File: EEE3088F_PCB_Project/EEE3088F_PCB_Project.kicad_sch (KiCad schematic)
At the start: 47 parts, among them IC1 DRV8833PWPR, IC2 DRV8833PWPR, IC3 TPS62067DSGR, IC4 TPS62067DSGR, IC5 INA219AIDCNR, IC6 XL1509-5.0E1, IC7 TPS61088RHLR, J1 Conn_02x16_Odd_Even, Q1 AO3400A, Q2 AO3400A, Q5 AO3401A, Q6 AO3401A

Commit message: v0.8
- updated voltage regulation circuit (still adjusting component values)
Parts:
- removed IC6: XL1509-5.0E1, SOIC127P600X175-8N, symbol XL1509-5_0E1:XL1509-5.0E1
- added C15: 47n, CAPC1608X90N, symbol CL10B473KB8NNNC:CL10B473KB8NNNC
- added C16, C17, C21, C22, C23, C24: C_Small, symbol Device:C_Small
- added C18, C19, C7: 100n, CAPC3216X100N, symbol CL31B104KBCNNNC:CL31B104KBCNNNC
- added C2: 2.2µ, CAPC3216X180N, symbol CL31B225KBHNNNE:CL31B225KBHNNNE
- added C20: 10µ, CAPC3216X180N, symbol CL31A106KBHNNNE:CL31A106KBHNNNE
- added L2: 1.2µ, symbol Device:L_Small
- added R10: 100k, 1206W4F1003T5E:RESC3115X65N, symbol 1206W4F1003T5E:1206W4F1003T5E
- added R11, R16: R_Small_US, symbol Device:R_Small_US
- added R12: 255k, symbol Device:R_Small_US
- added R13: 56k, symbol Device:R_Small_US
- J1: now left out of the parts list
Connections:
- net 3V3 OUT: now also C7.1; no longer IC5.4 (VS)
- net 5V OUT: now also IC7.14 (VOUT_1), C21.1, C22.1, C23.1, C24.1, R16.1
- net BATTERY: now also IC7.2 (EN), IC7.9 (VBN), C18.2, C20.1, L2.2
- net GND: now also IC7.11 (NC_1), IC7.12 (NC_2), IC7.13 (MODE), IC7.20 (AGND), IC7.21 (PGND), C15.1, C17.1, C18.1, C2.1, C20.2, C21.2, C22.2, C23.2, C24.2, R10.1, R13.1
- net at IC7.1 (VCC): now also C2.2
- net at IC7.10 (SS): now also C15.2
- net at IC7.17 (FB): now also R13.2, R16.2
- net at IC7.18 (COMP): now also C16.2, R11.2
- net at IC7.19 (ILIM): now also R10.2
- net at IC7.3 (FSW): now also R12.1
- net at IC7.4 (SW_1): now also C19.1, L2.1, R12.2
- net at IC7.8 (BOOT): now also C19.2
- net RESV: no longer names the net of J1.15 (Pin_15)
- new net: C16.1, C17.2, R11.1
- new net: C7.2, IC5.4 (VS)
- no-connect marks 0 -> 6
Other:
- note added: "Voltage Regulation"
- note removed: "Voltage Regulation v1"
- moved on the sheet: C1, C11, C12, C3, C4, C8, IC3, IC4, IC5, IC7, L1, L3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

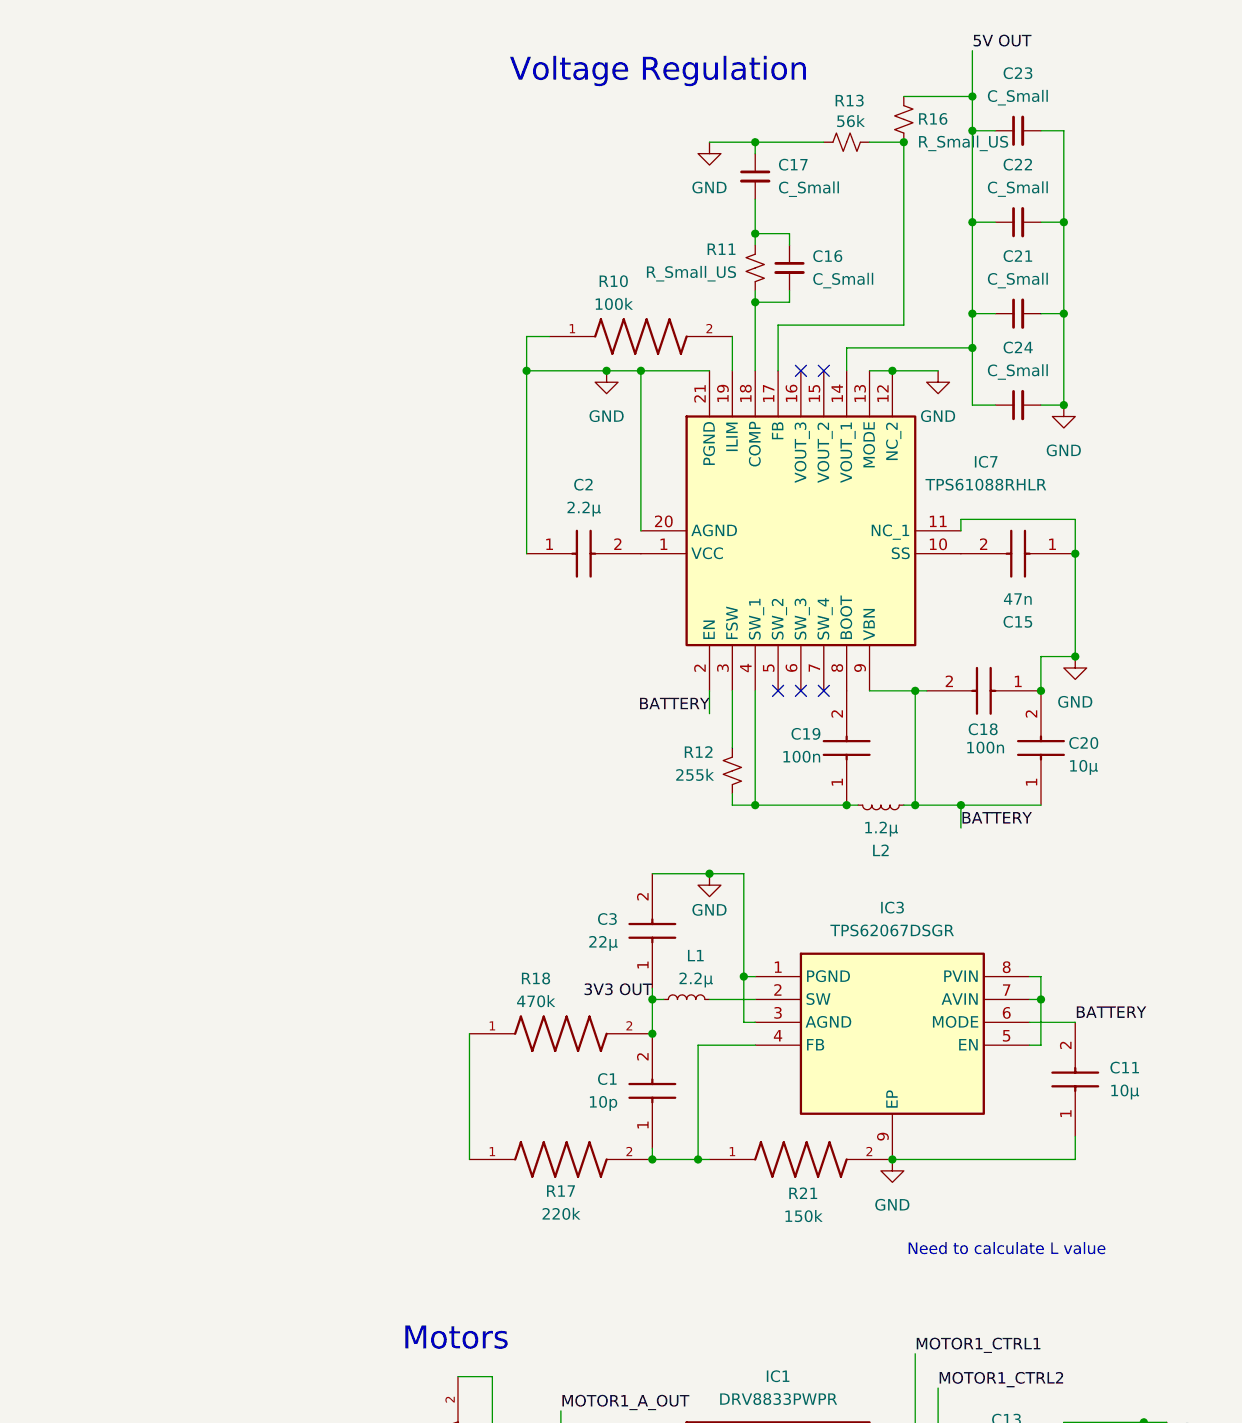
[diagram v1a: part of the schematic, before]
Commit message: v0.8.1
Voltage regulator components updated
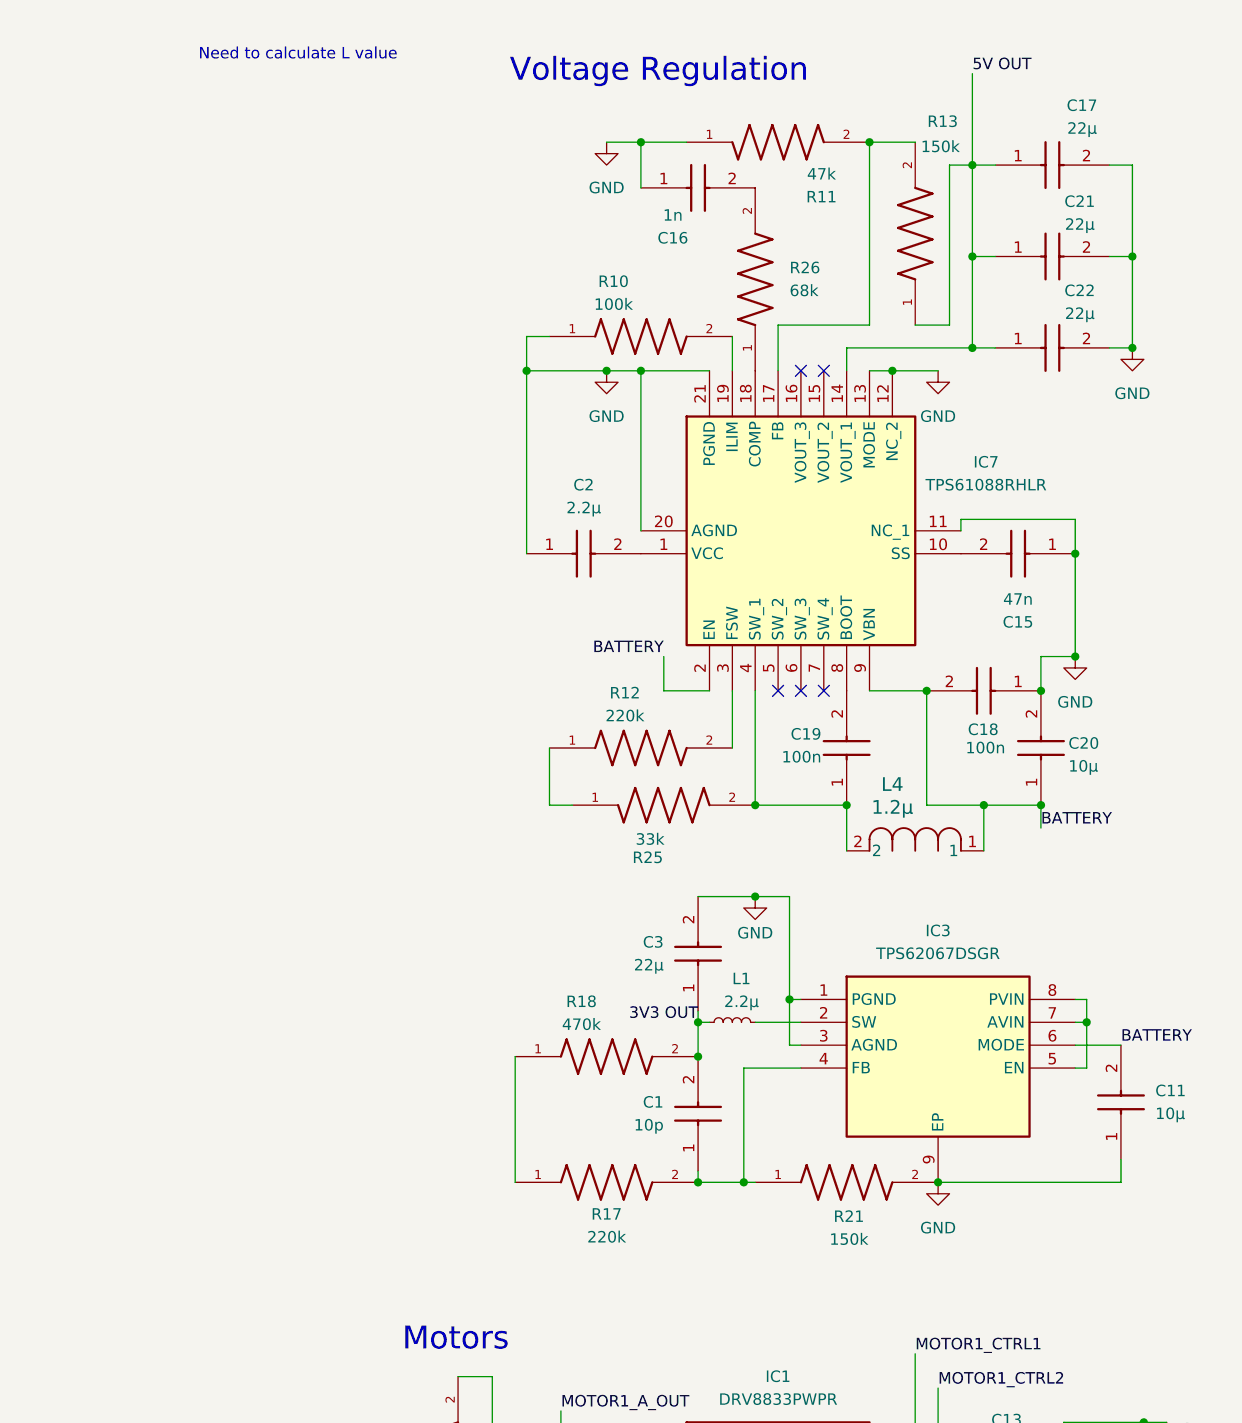
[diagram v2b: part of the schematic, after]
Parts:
- removed C16, C17, C21, C22, C23, C24: C_Small, symbol Device:C_Small
- removed L2: 1.2µ, symbol Device:L_Small
- removed R11, R16: R_Small_US, symbol Device:R_Small_US
- removed R12: 255k, symbol Device:R_Small_US
- removed R13: 56k, symbol Device:R_Small_US
- added C16: 1n, CAPC3215X163N, symbol 1206B102K202NT:1206B102K202NT
- added C17, C21, C22: 22µ, CAPC3216X180N, symbol CL31A226KAHNNNE:CL31A226KAHNNNE
- added L4: 1.2µ, IND_FXL0420_CMT, symbol 2025-03-28_01-51-26:FXL0420-6R8-M
- added R11: 47k, 0805W8F4702T5E:RESC2012X65N, symbol 0805W8F4702T5E:0805W8F4702T5E
- added R12: 220k, 0805W8F2203T5E:RESC2012X65N, symbol 0805W8F2203T5E:0805W8F2203T5E
- added R13: 150k, 0805W8F1503T5E:RESC2012X65N, symbol 0805W8F1503T5E:0805W8F1503T5E
- added R25: 33k, 0805W8F3302T5E:RESC2012X65N, symbol 0805W8F3302T5E:0805W8F3302T5E
- added R26: 68k, 0805W8F6802T5E:RESC2012X65N, symbol 0805W8F6802T5E:0805W8F6802T5E
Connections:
- net 5V OUT: now also C17.1, C21.1, C22.1, R13.1
- net BATTERY: now also L4.1
- net GND: now also C16.1, C17.2, C21.2, C22.2, R11.1
- net at IC7.17 (FB): now also R11.2, R13.2
- net at IC7.18 (COMP): now also R26.1
- net at IC7.3 (FSW): now also R12.2
- net at C19.1, IC7.4 (SW_1): now also L4.2, R25.2
- new net: C16.2, R26.2
- new net: R12.1, R25.1
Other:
- moved on the sheet: C1, C11, C3, IC3, L1, R17, R18, R21

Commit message: v0.9
Created my circuits in KiCad
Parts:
- added C23: 1u, symbol CL31B105KBHNNNE:CL31B105KBHNNNE
- added C24: 10u, CAPC3216X180N, symbol CL31A106KBHNNNE:CL31A106KBHNNNE
- added J2: TYPE-C16PIN, CONN16_C16PIN_SHN, symbol TYPE C16PIN:TYPE-C16PIN
- added L2: 2u2, symbol FHW0805UF2R2JST:FHW0805UF2R2JST
- added LED1: 0805G (Green), symbol KT-0805G:0805G (Green)
- added LED2: KT-0603R, symbol KT-0603R:KT-0603R
- added R16: 5k6, symbol SCHLIB_0402WGF5601TCE_2025-03-28:0402WGF5601TCE
- added R27: 3k3, symbol 0402WGF3301TCE:0402WGF3301TCE
- added R28, R30: 1k, symbol 0402WGF1001TCE:0402WGF1001TCE
- added R29: 75k, symbol 0603WAF7502T5E:0603WAF7502T5E
- added SW1: 1MS1T1B1M2QES, 1MS1T1_DYW, symbol 1MS1TIB1M2QES:1MS1T1B1M2QES
- added U1: HUSB237-AA001-DN06R, symbol HUSB237-AA001-DN06R:HUSB237-AA001-DN06R
- added U2: SLM6600, SOP8_4X5P1-1P27_SOI, symbol SLM6600:SLM6600
- added U3: IRLML6344TRPBF, IRLML6344TRPBF_INF, symbol IRLML6344TRPBF:IRLML6344TRPBF
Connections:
- net BATTERY: now also R28.2, SW1.1
- net FAST_CHARGE_CTRL: now also U3.1 (G)
- net GND: now also C23.1, C24.2, J2.B1 (GND), J2.B12 (GND), J2.S1 (SHELL_GND), J2.S2 (SHELL_GND), J2.S3 (SHELL_GND), J2.S4 (SHELL_GND), L2.2, R16.2, R27.2, R28.1, R29.1, SW1.3, U1.7 (GND), U2.6 (BAT), U2.7 (GND)
- net HV: now also C23.2, C24.1, J2.B4 (VBUS), J2.B9 (VBUS), R30.2, U1.2 (VUSB), U2.1 (VCC), U2.5 (TS)
- new net: LED2.1 (K), U2.4 (NCHRG)
- new net: LED1.1 (A), LED2.2 (A), R30.1
- new net: R27.1, U3.2 (S)
- new net: LED1.2 (K), U2.3 (NSTDBY)
- new net: R29.2, U1.3 (VSET)
- new net: L2.1, U2.8 (LX)
- new net CC1: J2.A5 (CC1), U1.1 (CC1)
- new net CC2: J2.B5 (CC2), U1.6 (CC2)
- new net D+: J2.A6 (DP1), J2.B6 (DP2), U1.4 (D+)
- new net D-: J2.A7 (DN1), J2.B7 (DN2), U1.5 (D-)
- new net PROG: R16.1, U2.2 (PROG), U3.3 (D)
- new net V-REG: SW1.2
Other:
- note added: "Battery Management"
- note added: "ON/OFF SWITCH"
- note added: "Power Negotiation"

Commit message: v1.0
Changed V-REG to PWR SWITCH OUT
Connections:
- net V-REG renamed PWR SWITCH OUT
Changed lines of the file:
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@@
 		)
 	)
-	(label "V-REG"
+	(label "PWR SWITCH OUT"
 		(at 125.73 63.5 0)
 		(effects
@@
 		(polyline
 			(pts
-				(xy 316.103 155.194) (xy 403.733 155.194) (xy 404.241 15.494) (xy 316.611 15.494)
+				(xy 15.875 229.87) (xy 66.04 229.87) (xy 66.04 280.67) (xy 15.875 280.67)
+			)
+			(stroke
+				(width 0)
+				(type dash)
+			)
+			(fill
+				(type none)
+			)
+		)
+	)
+	(rule_area
+		(polyline
+			(pts
+				(xy 163.83 227.33) (xy 163.83 280.67) (xy 229.87 280.67) (xy 229.87 227.33)
 			)
 			(stroke
@@
 		(polyline
 			(pts
-				(xy 15.875 229.87) (xy 66.04 229.87) (xy 66.04 280.67) (xy 15.875 280.67)
+				(xy 316.103 155.194) (xy 403.733 155.194) (xy 404.241 15.494) (xy 316.611 15.494)
 			)
 			(stroke
-				(width 0)
-				(type dash)
-			)
-			(fill
-				(type none)
-			)
-		)
-	)
-	(rule_area
-		(polyline
-			(pts
-				(xy 163.83 227.33) (xy 163.83 280.67) (xy 229.87 280.67) (xy 229.87 227.33)
-			)
-			(stroke

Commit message: v1.1
All circuit schematics done
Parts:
- removed C12: 10µ, CAPC3216X180N, symbol CL31A106KBHNNNE:CL31A106KBHNNNE
- removed C4: 22µ, CAPC2012X140N, symbol CL21A226MAQNNNE:CL21A226MAQNNNE
- removed C8: 10p, symbol Device:C_Small
- removed IC4: TPS62067DSGR, SON50P200X200X80-9N, symbol TPS62067DSGR:TPS62067DSGR
- removed L1, L3: 2.2µ, symbol Device:L_Small
- removed R1: 120k, 0603WAF1203T5E:RESC1608X55N, symbol 0603WAF1203T5E:0603WAF1203T5E
- removed R2: 39k, 0603WAF3902T5E:RESC1608X55N, symbol 0603WAF3902T5E:0603WAF3902T5E
- removed R22: 150k, 0805W8F1503T5E:RESC2012X65N, symbol 0805W8F1503T5E:0805W8F1503T5E
- removed R23: 470k, 0805W8F4703T5E:RESC2012X65N, symbol 0805W8F4703T5E:0805W8F4703T5E
- removed R24: 220k, 0805W8F2203T5E:RESC2012X65N, symbol 0805W8F2203T5E:0805W8F2203T5E
- added J3: Conn_01x02, Connector_JST:JST_PH_S2B-PH-K_1x02_P2.00mm_Horizontal, symbol Connector_Generic:Conn_01x02
- added L3: 2u2, symbol FHW0805UF2R2JST:FHW0805UF2R2JST
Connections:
- net 3V3 OUT: now also L3.1
- net BATTERY: now also J3.1 (Pin_1); no longer C11.2, C18.2, C20.1, IC3.6 (MODE), IC7.2 (EN), IC7.9 (VBN), L4.1, SW1.1
- net GND: now also J3.2 (Pin_2), L3.2
- net PWR SWITCH IN: now also SW1.1
- net PWR SWITCH OUT: now also C11.2, C18.2, C20.1, IC3.6 (MODE), IC7.2 (EN), IC7.9 (VBN), L4.1
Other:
- note removed: "Battery Charging"
- note removed: "Check where resistors necessary. Isen = 200mV / RIsen for 200mA -> 1Ω for 500mA -> 0.4Ω bypass ceramic cap: min 10µF (VM) bypass cap: 2.2µF, 6.3V (VINT) ceramic cap: 0.01-μF, 16-V (minimum) X7R (VCP)"
- note removed: "Do not populate: - 2x16 pin connector - battery"
- note removed: "Need to calculate L value"
- note removed: "Power Switch"
- note removed: "USB-C"
- note removed: "order extra 50mΩ"
- moved on the sheet: C1, C11, C15, C16, C17, C18, C19, C2, C20, C21, C22, C3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

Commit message: v1.2
Starting with PCB design
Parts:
- removed L3: 2u2, symbol FHW0805UF2R2JST:FHW0805UF2R2JST
- added L5: 1.2µ, IND_FXL0420_CMT, symbol 2025-03-28_01-51-26:FXL0420-6R8-M
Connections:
- net 3V3 OUT: now also L5.2
- net at IC3.2 (SW): now also L5.1
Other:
- moved on the sheet: C1, C3, R17, R18
